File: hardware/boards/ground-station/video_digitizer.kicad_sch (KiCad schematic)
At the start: 31 parts, among them U601 ADV7282A-M, U602 AP2127K-1.8, U603 AP2127K-1.8, Y601 28.63636 MHz

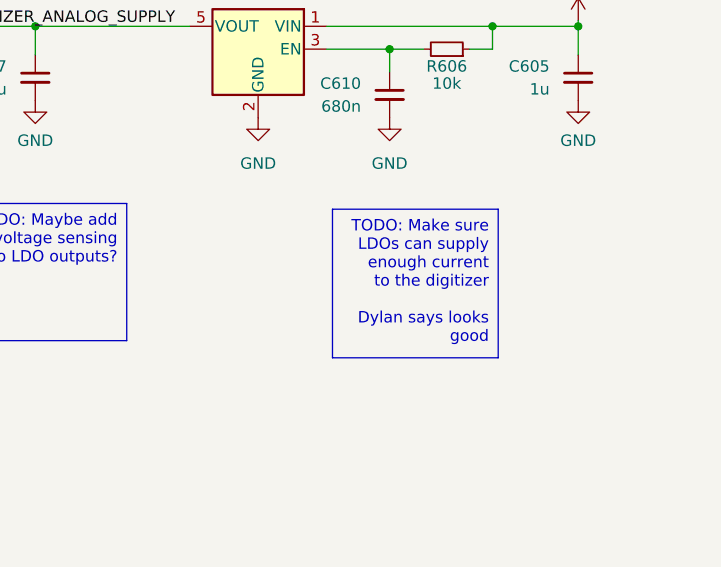
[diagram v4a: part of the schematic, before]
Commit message: Add TVS diode on 5V rail
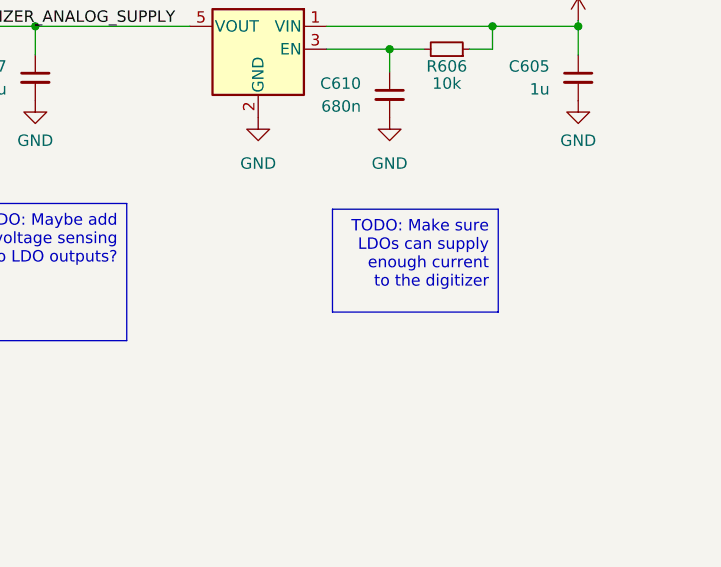
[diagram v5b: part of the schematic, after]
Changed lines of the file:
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@@
     )
   )
-  (text_box "TODO: Make sure LDOs can supply enough current to the digitizer\n\nDylan says looks good"
-    (at 222.25 68.58 0) (size 18.415 16.51)
+  (text_box "TODO: Make sure LDOs can supply enough current to the digitizer"
+    (at 222.25 68.58 0) (size 18.415 11.43)
     (stroke (width 0) (type default))
     (fill (type color) (color 255 255 0 1))

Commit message: sch review
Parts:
- removed C601: 100n, symbol Device:C_Small
- removed C609: 680n, symbol Device:C_Small
- removed R601: 24R, symbol Device:R_Small
- removed R602: 21R, symbol Device:R_Small
- removed R607: 10k, symbol Device:R_Small
- added C3: 100n, symbol Device:C_Small
- added R22, R27, R28, R6: 0, symbol Device:R_Small
- added R4: 24R, symbol Device:R_Small
- added R5: 51R, symbol Device:R_Small
- added TP3: TestPoint, symbol Connector:TestPoint
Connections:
- net +3V3: now also R27.1
- net ANALOG_VIDEO: now also R4.1
- net GND: now also R22.1, R28.1, R5.2, R6.1; no longer U601.29 (ALSB)
- net VID_EN_1V8: now reaches C610.1, R606.2, U603.3 (EN)
- net VID_EN_1V8: now also U602.3 (EN)
- net at U601.17 (AIN1): now also C3.2
- net at U601.18 (AIN2): now also TP3.1
- net at U601.22 (DIAG1): now also R6.2
- net at U601.25 (DIAG2): now also R22.2
- new net: C3.1, R4.2, R5.1
- new net: R27.2, R28.2, U601.29 (ALSB)
- no-connect marks 10 -> 7
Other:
- moved on the sheet: C604, R606

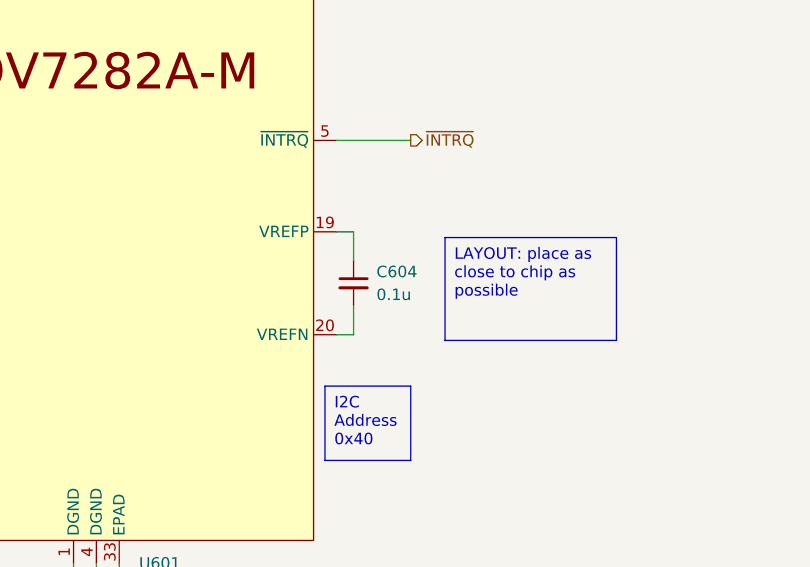
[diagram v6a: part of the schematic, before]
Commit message: Added footprints for most things
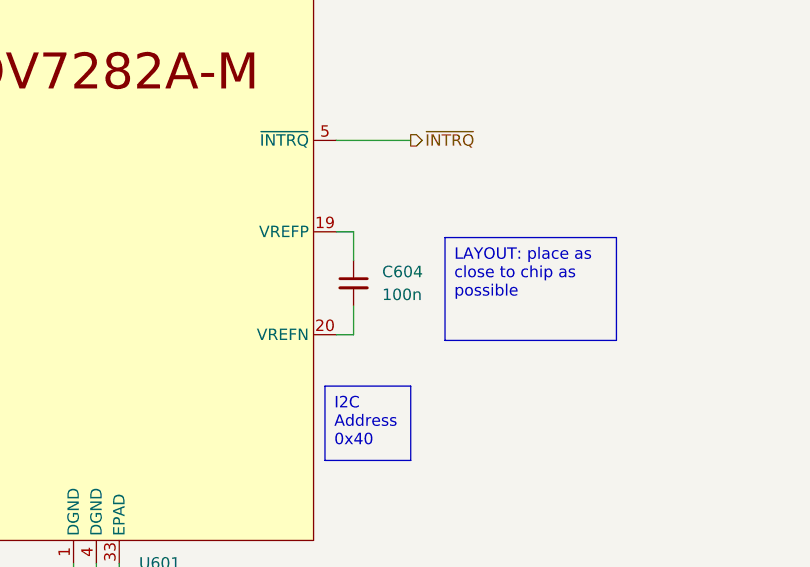
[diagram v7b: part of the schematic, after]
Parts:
- C3, C602, C603, C611, C612, C613, C614, C615, C616, C617, C618, C619, C620: footprint (none) -> Capacitor_SMD:C_0201_0603Metric
- C604: value 0.1u -> 100n; footprint (none) -> Capacitor_SMD:C_0201_0603Metric
- C605, C606, C607, C608, C610: footprint (none) -> Capacitor_SMD:C_0402_1005Metric
- R22, R27, R28, R6: footprint (none) -> Resistor_SMD:R_0402_1005Metric
- R4, R5: footprint (none) -> Resistor_SMD:R_0603_1608Metric
- R603, R604, R605, R606: footprint (none) -> Resistor_SMD:R_0201_0603Metric
- TP3: footprint (none) -> TestPoint:TestPoint_THTPad_D2.5mm_Drill1.2mm
- U601: footprint (none) -> Package_DFN_QFN:QFN-32-1EP_5x5mm_P0.5mm_EP3.6x3.6mm
- Y601: footprint (none) -> Crystal:Crystal_SMD_Abracon_ABM3-2Pin_5.0x3.2mm
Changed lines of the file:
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@@
       (effects (font (size 1.27 1.27)))
     )
-    (property "Footprint" "" (at 93.98 111.125 0)
+    (property "Footprint" "Resistor_SMD:R_0402_1005Metric" (at 93.98 111.125 0)
       (effects (font (size 1.27 1.27)) hide)
     )
@@
       (effects (font (size 1.27 1.27)) hide)
     )
-    (pin "2")
-    (pin "1")
+    (pin "1")
+    (pin "2")
     (instances
       (project "ground-station"
@@
       (effects (font (size 1.27 1.27)))
     )
-    (property "Footprint" "" (at 92.71 136.525 0)
+    (property "Footprint" "Resistor_SMD:R_0201_0603Metric" (at 92.71 136.525 0)
       (effects (font (size 1.27 1.27)) hide)
     )
@@
       (effects (font (size 1.27 1.27)) (justify left))
     )
-    (property "Footprint" "" (at 189.23 53.975 0)
+    (property "Footprint" "Capacitor_SMD:C_0402_1005Metric" (at 189.23 53.975 0)
       (effects (font (size 1.27 1.27)) hide)
     )
@@
       (effects (font (size 1.27 1.27)) (justify left))
     )
-    (property "Footprint" "" (at 53.975 173.355 0)
+    (property "Footprint" "Resistor_SMD:R_0201_0603Metric" (at 53.975 173.355 0)
       (effects (font (size 1.27 1.27)) hide)
     )
@@
       (effects (font (size 1.27 1.27)))
     )
-    (property "Footprint" "" (at 235.585 50.8 0)
+    (property "Footprint" "Resistor_SMD:R_0201_0603Metric" (at 235.585 50.8 0)
       (effects (font (size 1.27 1.27)) hide)
     )
@@
       (effects (font (size 1.27 1.27)) (justify left))
     )
-    (property "Footprint" "" (at 92.71 55.88 0)
+    (property "Footprint" "Capacitor_SMD:C_0201_0603Metric" (at 92.71 55.88 0)
       (effects (font (size 1.27 1.27)) hide)
     )
@@
       (effects (font (size 1.27 1.27)))
     )
-    (property "Footprint" "" (at 86.36 79.375 0)
+    (property "Footprint" "Capacitor_SMD:C_0201_0603Metric" (at 86.36 79.375 0)
       (effects (font (size 1.27 1.27)) hide)
     )
@@
       (effects (font (size 1.27 1.27)) (justify left))
     )
-    (property "Footprint" "" (at 228.6 55.88 0)
+    (property "Footprint" "Capacitor_SMD:C_0402_1005Metric" (at 228.6 55.88 0)
       (effects (font (size 1.27 1.27)) hide)
     )
@@
       (effects (font (size 1.27 1.27)) hide)
     )
-    (property "Footprint" "" (at 95.885 80.645 0)
+    (property "Footprint" "TestPoint:TestPoint_THTPad_D2.5mm_Drill1.2mm" (at 95.885 80.645 0)
       (effects (font (size 1.27 1.27)) hide)
     )
@@
       (effects (font (size 1.27 1.27)) (justify left))
     )
-    (property "Footprint" "" (at 20.32 24.13 0)
+    (property "Footprint" "Capacitor_SMD:C_0402_1005Metric" (at 20.32 24.13 0)
       (effects (font (size 1.27 1.27)) hide)
     )
@@
       (effects (font (size 1.27 1.27)) (justify left))
     )
-    (property "Footprint" "" (at 130.81 34.925 0)
+    (property "Footprint" "Capacitor_SMD:C_0201_0603Metric" (at 130.81 34.925 0)
       (effects (font (size 1.27 1.27)) hide)
     )
@@
       (effects (font (size 1.27 1.27)) (justify left))
     )
-    (property "Footprint" "" (at 79.375 24.765 0)
+    (property "Footprint" "Capacitor_SMD:C_0402_1005Metric" (at 79.375 24.765 0)
       (effects (font (size 1.27 1.27)) hide)
     )
@@
       (effects (font (size 1.27 1.27)))
     )
-    (property "Footprint" "" (at 73.025 79.375 0)
+    (property "Footprint" "Resistor_SMD:R_0603_1608Metric" (at 73.025 79.375 0)
       (effects (font (size 1.27 1.27)) hide)
     )
@@
       (effects (font (size 1.27 1.27)))
     )
-    (property "Footprint" "" (at 68.58 147.955 0)
+    (property "Footprint" "Capacitor_SMD:C_0201_0603Metric" (at 68.58 147.955 0)
       (effects (font (size 1.27 1.27)) hide)
     )
@@
       (effects (font (size 1.27 1.27)) (justify left))
     )
-    (property "Footprint" "" (at 140.335 34.925 0)
+    (property "Footprint" "Capacitor_SMD:C_0201_0603Metric" (at 140.335 34.925 0)
       (effects (font (size 1.27 1.27)) hide)
     )
@@
       (effects (font (size 1.27 1.27)) (justify left))
     )
-    (property "Footprint" "" (at 40.64 173.355 0)
+    (property "Footprint" "Resistor_SMD:R_0201_0603Metric" (at 40.64 173.355 0)
       (effects (font (size 1.27 1.27)) hide)
     )
@@
       (effects (font (size 1.27 1.27)))
     )
-    (property "Footprint" "" (at 81.28 155.575 0)
+    (property "Footprint" "Resistor_SMD:R_0402_1005Metric" (at 81.28 155.575 0)
       (effects (font (size 1.27 1.27)) hide)
     )
@@
       (effects (font (size 1.27 1.27)) hide)
     )
-    (pin "2")
-    (pin "1")
+    (pin "1")
+    (pin "2")
     (instances
       (project "ground-station"
@@
       (effects (font (size 1.27 1.27)) (justify left))
     )
-    (property "Footprint" "" (at 137.16 52.07 0)
+    (property "Footprint" "Capacitor_SMD:C_0201_0603Metric" (at 137.16 52.07 0)
       (effects (font (size 1.27 1.27)) hide)
     )
@@
       (effects (font (size 1.27 1.27)) (justify left))
     )
-    (property "Footprint" "" (at 163.83 62.865 0)
+    (property "Footprint" "Capacitor_SMD:C_0201_0603Metric" (at 163.83 62.865 0)
       (effects (font (size 1.27 1.27)) hide)
     )
@@
       (effects (font (size 1.27 1.27)) (justify left))
     )
-    (property "Footprint" "" (at 154.94 62.865 0)
+    (property "Footprint" "Capacitor_SMD:C_0201_0603Metric" (at 154.94 62.865 0)
       (effects (font (size 1.27 1.27)) hide)
     )
@@
       (effects (font (size 1.27 1.27)))
     )
-    (property "Footprint" "" (at 92.71 158.75 0)
+    (property "Footprint" "Resistor_SMD:R_0402_1005Metric" (at 92.71 158.75 0)
       (effects (font (size 1.27 1.27)) hide)
     )
@@
       (effects (font (size 1.27 1.27)) hide)
     )
-    (pin "2")
-    (pin "1")
+    (pin "1")
+    (pin "2")
     (instances
       (project "ground-station"
@@
       (effects (font (size 1.27 1.27)))
     )
-    (property "Footprint" "" (at 93.98 92.075 0)
+    (property "Footprint" "Resistor_SMD:R_0402_1005Metric" (at 93.98 92.075 0)
       (effects (font (size 1.27 1.27)) hide)
     )
@@
       (effects (font (size 1.27 1.27)) hide)
     )
-    (pin "2")
-    (pin "1")
+    (pin "1")
+    (pin "2")
     (instances
       (project "ground-station"
@@
       (effects (font (size 1.27 1.27)) (justify right))
     )
-    (property "Footprint" "" (at 81.28 142.24 0)
+    (property "Footprint" "Crystal:Crystal_SMD_Abracon_ABM3-2Pin_5.0x3.2mm" (at 81.28 142.24 0)
       (effects (font (size 1.27 1.27)) hide)
     )
@@
       (effects (font (size 1.27 1.27)))
     )
-    (property "Footprint" "" (at 68.58 136.525 0)
+    (property "Footprint" "Capacitor_SMD:C_0201_0603Metric" (at 68.58 136.525 0)
       (effects (font (size 1.27 1.27)) hide)
     )
@@
       (effects (font (size 1.27 1.27)) (justify left))
     )
-    (property "Footprint" "" (at 100.965 37.465 0)
+    (property "Footprint" "Capacitor_SMD:C_0201_0603Metric" (at 100.965 37.465 0)
       (effects (font (size 1.27 1.27)) hide)
     )
@@
       (effects (font (size 1.27 1.27)) (justify left))
     )
-    (property "Footprint" "" (at 77.47 83.82 0)
+    (property "Footprint" "Resistor_SMD:R_0603_1608Metric" (at 77.47 83.82 0)
       (effects (font (size 1.27 1.27)) hide)
     )
@@
       (effects (font (size 1.27 1.27)) (justify left))
     )
-    (property "Footprint" "" (at 147.32 52.07 0)
+    (property "Footprint" "Capacitor_SMD:C_0201_0603Metric" (at 147.32 52.07 0)
       (effects (font (size 1.27 1.27)) hide)
     )
@@
       (effects (font (size 1.27 1.27)) (justify left))
     )
-    (property "Footprint" "" (at 110.49 37.465 0)
+    (property "Footprint" "Capacitor_SMD:C_0201_0603Metric" (at 110.49 37.465 0)
       (effects (font (size 1.27 1.27)) hide)
     )
@@
       (effects (font (size 1.27 1.27)) (justify left))
     )
-    (property "Footprint" "" (at 102.87 55.88 0)
+    (property "Footprint" "Capacitor_SMD:C_0201_0603Metric" (at 102.87 55.88 0)
       (effects (font (size 1.27 1.27)) hide)
     )
@@
   (symbol (lib_id "Device:C_Small") (at 154.305 154.94 0) (unit 1)
     (in_bom yes) (on_board yes) (dnp no) (fields_autoplaced)
-    (property "Reference" "C604" (at 156.845 153.6763 0)
-      (effects (font (size 1.27 1.27)) (justify left))
-    )
-    (property "Value" "0.1u" (at 156.845 156.2163 0)
-      (effects (font (size 1.27 1.27)) (justify left))
-    )
-    (property "Footprint" "" (at 154.305 154.94 0)
+    (property "Reference" "C604" (at 157.48 153.6763 0)
+      (effects (font (size 1.27 1.27)) (justify left))
+    )
+    (property "Value" "100n" (at 157.48 156.2163 0)
+      (effects (font (size 1.27 1.27)) (justify left))
+    )
+    (property "Footprint" "Capacitor_SMD:C_0201_0603Metric" (at 154.305 154.94 0)
       (effects (font (size 1.27 1.27)) hide)
     )
@@
       (effects (font (size 1.27 1.27)))
     )
-    (property "Footprint" "" (at 127 117.475 0)
+    (property "Footprint" "Package_DFN_QFN:QFN-32-1EP_5x5mm_P0.5mm_EP3.6x3.6mm" (at 127 117.475 0)
       (effects (font (size 1.27 1.27)) hide)
     )
@@
       (effects (font (size 1.27 1.27)) (justify left))
     )
-    (property "Footprint" "" (at 249.555 53.975 0)
-      (effects (font (size 1.27 1.27)) hide)
-    )
+    (property "Footprint" "Capacitor_SMD:C_0402_1005Metric" (at 249.555 53.975 0)
+      (effects (font (size 1.27 1.27)) hide)
+    )
